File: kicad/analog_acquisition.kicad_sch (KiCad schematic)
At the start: 59 parts, among them J2 BNC_Isolated, J3 BNC_Isolated, J4 JST-XH 3-pin, J5 BNC_Isolated, J6 JST-XH 2-pin, J7 JST-XH 3-pin, T1 Transformer_SP_2S, T2 Transformer_SP_2S, T3 Transformer_SP_2S, U10 MCP6002, U11 MCP6002, U12 SN6501, U13 AMC1301, U4 MCP6002, U5 SN6501, U6 AMC1301, U7 MCP6002, U8 SN6501, U9 AMC1301

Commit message: fix: Resolve 4 Devin Review issues on analog_acquisition
1. Duplicate #PWR refs: renumbered 6 colliding GND symbols
   (#PWR36/37/38/40 duplicated across non-iso channels)
   to unique refs #PWR51-56

2. Transformer footprint+MPN: T1-T3 assigned
   Wuerth 750315371 (SN6501-compatible center-tapped
   transformer), footprint from KiCad stock library

3. Zero-length wires: removed 3 degenerate wires at
   hier_label positions for CO2/Temp/Hum channels

4. Missing MPN/Distributor_PN: added to D19-D24
   (BAT54,115 Schottky) and C28-C30 (GRM21BR61C106KE15L
   10uF MLCC)

ERC: Analog Acquisition = 0 violations, trace_net = 0 shorts
Co-Authored-By: Devin AI <158243242+devin-ai-integration[bot]@users.noreply.github.com>
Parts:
- C28, C29, C30: Distributor_PN (none) -> 490-6473-1-ND; MPN (none) -> GRM21BR61C106KE15L
- D19, D20, D21, D22, D23, D24: Distributor_PN (none) -> 1727-3752-1-ND; MPN (none) -> BAT54,115
- T1, T2, T3: footprint (none) -> Transformer_SMD:Transformer_Wuerth_750315371; Distributor_PN (none) -> 732-13596-1-ND; MPN (none) -> 750315371
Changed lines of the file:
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@@
     (property "Value" "Transformer_SP_2S" (at 243.84 71.12 0)
       (effects (font (size 1.27 1.27))))
-    (property "Footprint" "" (at 243.84 63.5 0)
+    (property "Footprint" "Transformer_SMD:Transformer_Wuerth_750315371" (at 243.84 63.5 0)
+      (effects (font (size 1.27 1.27)) hide))
+    (property "MPN" "750315371" (at 0 0 0)
+      (effects (font (size 1.27 1.27)) hide))
+    (property "Distributor_PN" "732-13596-1-ND" (at 0 0 0)
       (effects (font (size 1.27 1.27)) hide))
     (pin "1")
@@
     (property "Footprint" "Diode_SMD:D_SOD-123" (at 274.32 53.34 0)
       (effects (font (size 1.27 1.27)) hide))
+    (property "MPN" "BAT54,115" (at 0 0 0)
+      (effects (font (size 1.27 1.27)) hide))
+    (property "Distributor_PN" "1727-3752-1-ND" (at 0 0 0)
+      (effects (font (size 1.27 1.27)) hide))
     (pin "1")
     (pin "2")
@@
     (property "Footprint" "Diode_SMD:D_SOD-123" (at 274.32 73.66 0)
       (effects (font (size 1.27 1.27)) hide))
+    (property "MPN" "BAT54,115" (at 0 0 0)
+      (effects (font (size 1.27 1.27)) hide))
+    (property "Distributor_PN" "1727-3752-1-ND" (at 0 0 0)
+      (effects (font (size 1.27 1.27)) hide))
     (pin "1")
     (pin "2")
@@
       (effects (font (size 1.27 1.27))))
     (property "Footprint" "Capacitor_SMD:C_0805_2012Metric" (at 289.56 63.5 0)
+      (effects (font (size 1.27 1.27)) hide))
+    (property "MPN" "GRM21BR61C106KE15L" (at 0 0 0)
+      (effects (font (size 1.27 1.27)) hide))
+    (property "Distributor_PN" "490-6473-1-ND" (at 0 0 0)
       (effects (font (size 1.27 1.27)) hide))
     (pin "1")
@@
     (property "Value" "Transformer_SP_2S" (at 243.84 109.22 0)
       (effects (font (size 1.27 1.27))))
-    (property "Footprint" "" (at 243.84 101.6 0)
+    (property "Footprint" "Transformer_SMD:Transformer_Wuerth_750315371" (at 243.84 101.6 0)
+      (effects (font (size 1.27 1.27)) hide))
+    (property "MPN" "750315371" (at 0 0 0)
+      (effects (font (size 1.27 1.27)) hide))
+    (property "Distributor_PN" "732-13596-1-ND" (at 0 0 0)
       (effects (font (size 1.27 1.27)) hide))
     (pin "1")
@@
     (property "Footprint" "Diode_SMD:D_SOD-123" (at 274.32 91.44 0)
       (effects (font (size 1.27 1.27)) hide))
+    (property "MPN" "BAT54,115" (at 0 0 0)
+      (effects (font (size 1.27 1.27)) hide))
+    (property "Distributor_PN" "1727-3752-1-ND" (at 0 0 0)
+      (effects (font (size 1.27 1.27)) hide))
     (pin "1")
     (pin "2")
@@
     (property "Footprint" "Diode_SMD:D_SOD-123" (at 274.32 111.75999999999999 0)
       (effects (font (size 1.27 1.27)) hide))
+    (property "MPN" "BAT54,115" (at 0 0 0)
+      (effects (font (size 1.27 1.27)) hide))
+    (property "Distributor_PN" "1727-3752-1-ND" (at 0 0 0)
+      (effects (font (size 1.27 1.27)) hide))
     (pin "1")
     (pin "2")
@@
       (effects (font (size 1.27 1.27))))
     (property "Footprint" "Capacitor_SMD:C_0805_2012Metric" (at 289.56 101.6 0)
+      (effects (font (size 1.27 1.27)) hide))
+    (property "MPN" "GRM21BR61C106KE15L" (at 0 0 0)
+      (effects (font (size 1.27 1.27)) hide))
+    (property "Distributor_PN" "490-6473-1-ND" (at 0 0 0)
       (effects (font (size 1.27 1.27)) hide))
     (pin "1")
@@
     (property "Value" "Transformer_SP_2S" (at 243.84 185.42000000000002 0)
       (effects (font (size 1.27 1.27))))
-    (property "Footprint" "" (at 243.84 177.8 0)
+    (property "Footprint" "Transformer_SMD:Transformer_Wuerth_750315371" (at 243.84 177.8 0)
+      (effects (font (size 1.27 1.27)) hide))
+    (property "MPN" "750315371" (at 0 0 0)
+      (effects (font (size 1.27 1.27)) hide))
+    (property "Distributor_PN" "732-13596-1-ND" (at 0 0 0)
       (effects (font (size 1.27 1.27)) hide))
     (pin "1")
@@
     (property "Footprint" "Diode_SMD:D_SOD-123" (at 274.32 167.64000000000001 0)
       (effects (font (size 1.27 1.27)) hide))
+    (property "MPN" "BAT54,115" (at 0 0 0)
+      (effects (font (size 1.27 1.27)) hide))
+    (property "Distributor_PN" "1727-3752-1-ND" (at 0 0 0)
+      (effects (font (size 1.27 1.27)) hide))
     (pin "1")
     (pin "2")
@@
     (property "Footprint" "Diode_SMD:D_SOD-123" (at 274.32 187.96 0)
       (effects (font (size 1.27 1.27)) hide))
+    (property "MPN" "BAT54,115" (at 0 0 0)
+      (effects (font (size 1.27 1.27)) hide))
+    (property "Distributor_PN" "1727-3752-1-ND" (at 0 0 0)
+      (effects (font (size 1.27 1.27)) hide))
     (pin "1")
     (pin "2")
@@
     (property "Footprint" "Capacitor_SMD:C_0805_2012Metric" (at 289.56 177.8 0)
       (effects (font (size 1.27 1.27)) hide))
+    (property "MPN" "GRM21BR61C106KE15L" (at 0 0 0)
+      (effects (font (size 1.27 1.27)) hide))
+    (property "Distributor_PN" "490-6473-1-ND" (at 0 0 0)
+      (effects (font (size 1.27 1.27)) hide))
     (pin "1")
     (pin "2")
@@
   )
   (wire (pts (xy 99.06 127.0) (xy 162.56 127.0))
-    (stroke (width 0) (type default))
-  )
-  (wire (pts (xy 162.56 127.0) (xy 162.56 127.0))
     (stroke (width 0) (type default))
   )
@@
     (unit 1)
     (exclude_from_sim no) (in_bom no) (on_board no)
-    (property "Reference" "#PWR36" (at 46.99 208.27999999999997 0)
+    (property "Reference" "#PWR51" (at 46.99 208.27999999999997 0)
       (effects (font (size 1.27 1.27)) hide))
     (property "Value" "GND" (at 46.99 207.01 0)
@@
     (pin "1")
     (instances (project "nebula_qshield"
-      (path "/c6da75fc-541f-4933-b134-f5eb8982a11b/9688e820-0346-4732-9e7d-cc0365bc1e8b" (reference "#PWR36") (unit 1))))
+      (path "/c6da75fc-541f-4933-b134-f5eb8982a11b/9688e820-0346-4732-9e7d-cc0365bc1e8b" (reference "#PWR51") (unit 1))))
   )
   (wire (pts (xy 54.61 203.2) (xy 52.07 203.2))
@@
     (unit 1)
     (exclude_from_sim no) (in_bom no) (on_board no)
-    (property "Reference" "#PWR37" (at 68.58 217.17 0)
+    (property "Reference" "#PWR52" (at 68.58 217.17 0)
       (effects (font (size 1.27 1.27)) hide))
     (property "Value" "GND" (at 68.58 215.9 0)
@@
     (pin "1")
     (instances (project "nebula_qshield"
-      (path "/c6da75fc-541f-4933-b134-f5eb8982a11b/9688e820-0346-4732-9e7d-cc0365bc1e8b" (reference "#PWR37") (unit 1))))
+      (path "/c6da75fc-541f-4933-b134-f5eb8982a11b/9688e820-0346-4732-9e7d-cc0365bc1e8b" (reference "#PWR52") (unit 1))))
   )
   (wire (pts (xy 76.2 207.01) (xy 76.2 204.47))
@@
     (unit 1)
     (exclude_from_sim no) (in_bom no) (on_board no)
-    (property "Reference" "#PWR38" (at 76.2 219.70999999999998 0)
+    (property "Reference" "#PWR53" (at 76.2 219.70999999999998 0)
       (effects (font (size 1.27 1.27)) hide))
     (property "Value" "GND" (at 76.2 218.44 0)
@@
     (pin "1")
     (instances (project "nebula_qshield"
-      (path "/c6da75fc-541f-4933-b134-f5eb8982a11b/9688e820-0346-4732-9e7d-cc0365bc1e8b" (reference "#PWR38") (unit 1))))
+      (path "/c6da75fc-541f-4933-b134-f5eb8982a11b/9688e820-0346-4732-9e7d-cc0365bc1e8b" (reference "#PWR53") (unit 1))))
   )
   (wire (pts (xy 64.77 203.2) (xy 162.56 203.2))
     (stroke (width 0) (type default))
   )
-  (wire (pts (xy 162.56 203.2) (xy 162.56 203.2))
-    (stroke (width 0) (type default))
-  )
   (wire (pts (xy 20.32 238.76) (xy 22.86 238.76))
     (stroke (width 0) (type default))
@@
     (unit 1)
     (exclude_from_sim no) (in_bom no) (on_board no)
-    (property "Reference" "#PWR37" (at 17.78 243.84 0)
+    (property "Reference" "#PWR54" (at 17.78 243.84 0)
       (effects (font (size 1.27 1.27)) hide))
     (property "Value" "GND" (at 17.78 242.57000000000002 0)
@@
     (pin "1")
     (instances (project "nebula_qshield"
-      (path "/c6da75fc-541f-4933-b134-f5eb8982a11b/9688e820-0346-4732-9e7d-cc0365bc1e8b" (reference "#PWR37") (unit 1))))
+      (path "/c6da75fc-541f-4933-b134-f5eb8982a11b/9688e820-0346-4732-9e7d-cc0365bc1e8b" (reference "#PWR54") (unit 1))))
   )
   (wire (pts (xy 20.32 243.84) (xy 17.78 243.84))
@@
     (unit 1)
     (exclude_from_sim no) (in_bom no) (on_board no)
-    (property "Reference" "#PWR38" (at 46.99 246.38 0)
+    (property "Reference" "#PWR55" (at 46.99 246.38 0)
       (effects (font (size 1.27 1.27)) hide))
     (property "Value" "GND" (at 46.99 245.11 0)
@@
     (pin "1")
     (instances (project "nebula_qshield"
-      (path "/c6da75fc-541f-4933-b134-f5eb8982a11b/9688e820-0346-4732-9e7d-cc0365bc1e8b" (reference "#PWR38") (unit 1))))
+      (path "/c6da75fc-541f-4933-b134-f5eb8982a11b/9688e820-0346-4732-9e7d-cc0365bc1e8b" (reference "#PWR55") (unit 1))))
   )
   (wire (pts (xy 54.61 241.3) (xy 52.07 241.3))
@@
     (unit 1)
     (exclude_from_sim no) (in_bom no) (on_board no)
-    (property "Reference" "#PWR40" (at 68.58 255.26999999999998 0)
+    (property "Reference" "#PWR56" (at 68.58 255.26999999999998 0)
       (effects (font (size 1.27 1.27)) hide))
     (property "Value" "GND" (at 68.58 254.0 0)
@@
     (pin "1")
     (instances (project "nebula_qshield"
-      (path "/c6da75fc-541f-4933-b134-f5eb8982a11b/9688e820-0346-4732-9e7d-cc0365bc1e8b" (reference "#PWR40") (unit 1))))
+      (path "/c6da75fc-541f-4933-b134-f5eb8982a11b/9688e820-0346-4732-9e7d-cc0365bc1e8b" (reference "#PWR56") (unit 1))))
   )
   (wire (pts (xy 76.2 245.11) (xy 76.2 242.57000000000002))
@@
     (stroke (width 0) (type default))
   )
-  (wire (pts (xy 162.56 241.3) (xy 162.56 241.3))
-    (stroke (width 0) (type default))
-  )

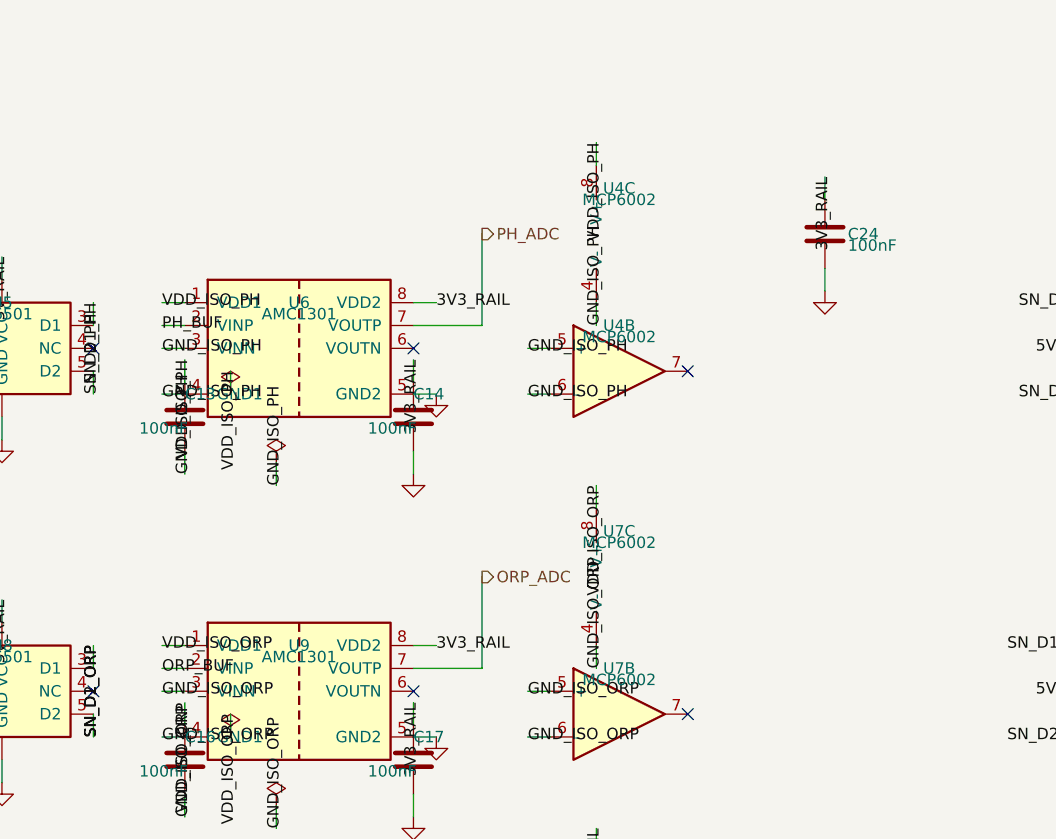
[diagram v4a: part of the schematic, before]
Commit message: fix: Add post-buffer resistive divider for pH/ORP input range (±250mV AMC1301)
Co-Authored-By: Devin AI <158243242+devin-ai-integration[bot]@users.noreply.github.com>
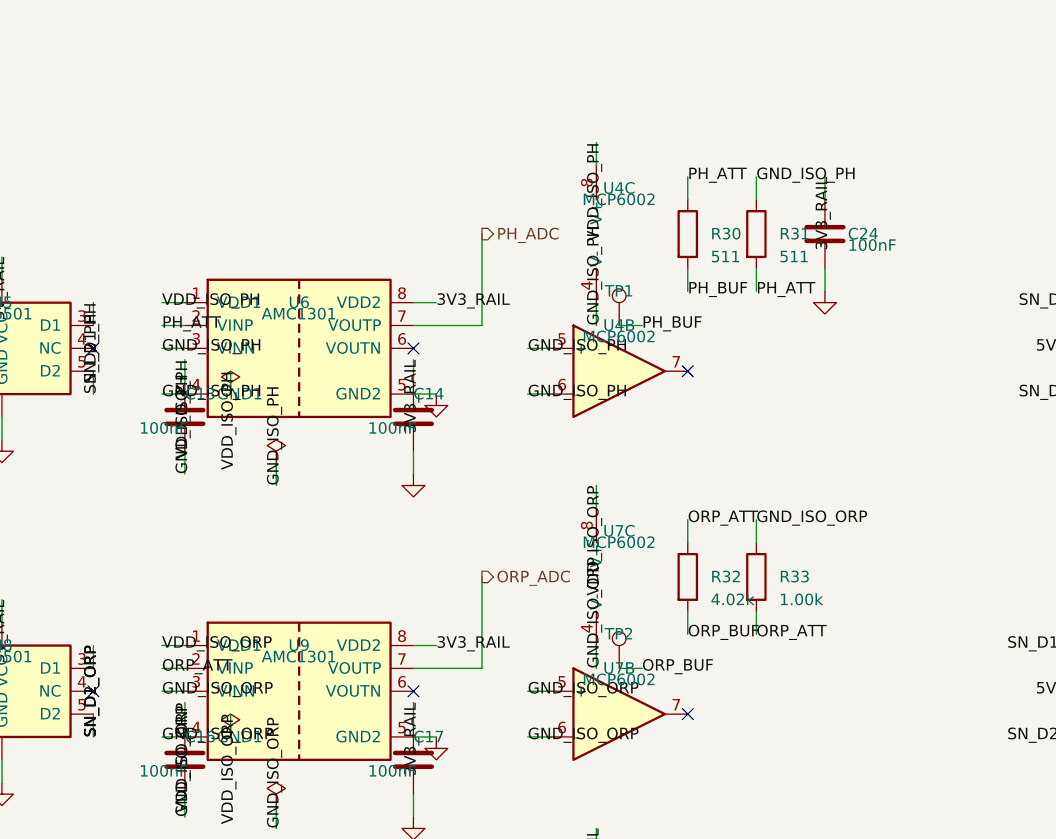
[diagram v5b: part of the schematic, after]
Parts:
- added R30, R31: 511, Resistor_SMD:R_0402_1005Metric, symbol Device:R
- added R32: 4.02k, Resistor_SMD:R_0402_1005Metric, symbol Device:R
- added R33: 1.00k, Resistor_SMD:R_0402_1005Metric, symbol Device:R
- added TP1, TP2: TestPoint, TestPoint:TestPoint_Pad_D1.5mm, symbol nebula_symbols:TestPoint
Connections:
- net GND_ISO_ORP: now also R33.1
- net GND_ISO_PH: now also R31.1
- net ORP_BUF: now also R32.2, TP2.1; no longer U9.2 (VINP)
- net PH_BUF: now also R30.2, TP1.1; no longer U6.2 (VINP)
- new net ORP_ATT: R32.1, R33.2, U9.2 (VINP)
- new net PH_ATT: R30.1, R31.2, U6.2 (VINP)
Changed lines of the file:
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@@
     (stroke (width 0) (type default))
   )
-  (label "PH_BUF" (at 126.99999999999999 60.96 0)
+  (label "PH_ATT" (at 126.99999999999999 60.96 0)
     (effects (font (size 1.27 1.27)))
   )
@@
     (stroke (width 0) (type default))
   )
-  (label "ORP_BUF" (at 126.99999999999999 99.06 0)
+  (label "ORP_ATT" (at 126.99999999999999 99.06 0)
     (effects (font (size 1.27 1.27)))
   )
@@
     (stroke (width 0) (type default))
   )
+  (symbol
+    (lib_id "Device:R")
+    (at 185.42 50.8 0)
+    (unit 1)
+    (exclude_from_sim no) (in_bom yes) (on_board yes)
+    (property "Reference" "R30" (at 187.95999999999998 50.8 0) (effects (font (size 1.27 1.27)) (justify left)))
+    (property "Value" "511" (at 187.95999999999998 53.339999999999996 0) (effects (font (size 1.27 1.27)) (justify left)))
+    (property "Footprint" "Resistor_SMD:R_0402_1005Metric" (at 185.42 50.8 90) (effects (font (size 1.27 1.27)) hide))
+    (property "Description" "pH input divider top (0.1%)" (at 185.42 50.8 0) (effects (font (size 1.27 1.27)) hide))
+    (pin "1") (pin "2")
+    (instances (project "nebula_qshield"
+      (path "/c6da75fc-541f-4933-b134-f5eb8982a11b/9688e820-0346-4732-9e7d-cc0365bc1e8b" (reference "R30") (unit 1))))
+  )
+  (wire (pts (xy 185.42 54.61) (xy 185.42 57.15)) (stroke (width 0) (type default)))
+  (label "PH_BUF" (at 185.42 57.15 0) (effects (font (size 1.27 1.27))))
+  (wire (pts (xy 185.42 46.989999999999995) (xy 185.42 44.449999999999996)) (stroke (width 0) (type default)))
+  (label "PH_ATT" (at 185.42 44.449999999999996 0) (effects (font (size 1.27 1.27))))
+  (symbol
+    (lib_id "Device:R")
+    (at 193.04 50.8 0)
+    (unit 1)
+    (exclude_from_sim no) (in_bom yes) (on_board yes)
+    (property "Reference" "R31" (at 195.57999999999998 50.8 0) (effects (font (size 1.27 1.27)) (justify left)))
+    (property "Value" "511" (at 195.57999999999998 53.339999999999996 0) (effects (font (size 1.27 1.27)) (justify left)))
+    (property "Footprint" "Resistor_SMD:R_0402_1005Metric" (at 193.04 50.8 90) (effects (font (size 1.27 1.27)) hide))
+    (property "Description" "pH input divider bottom (0.1%)" (at 193.04 50.8 0) (effects (font (size 1.27 1.27)) hide))
+    (pin "1") (pin "2")
+    (instances (project "nebula_qshield"
+      (path "/c6da75fc-541f-4933-b134-f5eb8982a11b/9688e820-0346-4732-9e7d-cc0365bc1e8b" (reference "R31") (unit 1))))
+  )
+  (wire (pts (xy 193.04 54.61) (xy 193.04 57.15)) (stroke (width 0) (type default)))
+  (label "PH_ATT" (at 193.04 57.15 0) (effects (font (size 1.27 1.27))))
+  (wire (pts (xy 193.04 46.989999999999995) (xy 193.04 44.449999999999996)) (stroke (width 0) (type default)))
+  (label "GND_ISO_PH" (at 193.04 44.449999999999996 0) (effects (font (size 1.27 1.27))))
+  (symbol
+    (lib_id "Device:R")
+    (at 185.42 88.9 0)
+    (unit 1)
+    (exclude_from_sim no) (in_bom yes) (on_board yes)
+    (property "Reference" "R32" (at 187.95999999999998 88.9 0) (effects (font (size 1.27 1.27)) (justify left)))
+    (property "Value" "4.02k" (at 187.95999999999998 91.44000000000001 0) (effects (font (size 1.27 1.27)) (justify left)))
+    (property "Footprint" "Resistor_SMD:R_0402_1005Metric" (at 185.42 88.9 90) (effects (font (size 1.27 1.27)) hide))
+    (property "Description" "ORP input divider top (0.1%)" (at 185.42 88.9 0) (effects (font (size 1.27 1.27)) hide))
+    (pin "1") (pin "2")
+    (instances (project "nebula_qshield"
+      (path "/c6da75fc-541f-4933-b134-f5eb8982a11b/9688e820-0346-4732-9e7d-cc0365bc1e8b" (reference "R32") (unit 1))))
+  )
+  (wire (pts (xy 185.42 92.71000000000001) (xy 185.42 95.25)) (stroke (width 0) (type default)))
+  (label "ORP_BUF" (at 185.42 95.25 0) (effects (font (size 1.27 1.27))))
+  (wire (pts (xy 185.42 85.09) (xy 185.42 82.55000000000001)) (stroke (width 0) (type default)))
+  (label "ORP_ATT" (at 185.42 82.55000000000001 0) (effects (font (size 1.27 1.27))))
+  (symbol
+    (lib_id "Device:R")
+    (at 193.04 88.9 0)
+    (unit 1)
+    (exclude_from_sim no) (in_bom yes) (on_board yes)
+    (property "Reference" "R33" (at 195.57999999999998 88.9 0) (effects (font (size 1.27 1.27)) (justify left)))
+    (property "Value" "1.00k" (at 195.57999999999998 91.44000000000001 0) (effects (font (size 1.27 1.27)) (justify left)))
+    (property "Footprint" "Resistor_SMD:R_0402_1005Metric" (at 193.04 88.9 90) (effects (font (size 1.27 1.27)) hide))
+    (property "Description" "ORP input divider bottom (0.1%)" (at 193.04 88.9 0) (effects (font (size 1.27 1.27)) hide))
+    (pin "1") (pin "2")
+    (instances (project "nebula_qshield"
+      (path "/c6da75fc-541f-4933-b134-f5eb8982a11b/9688e820-0346-4732-9e7d-cc0365bc1e8b" (reference "R33") (unit 1))))
+  )
+  (wire (pts (xy 193.04 92.71000000000001) (xy 193.04 95.25)) (stroke (width 0) (type default)))
+  (label "ORP_ATT" (at 193.04 95.25 0) (effects (font (size 1.27 1.27))))
+  (wire (pts (xy 193.04 85.09) (xy 193.04 82.55000000000001)) (stroke (width 0) (type default)))
+  (label "GND_ISO_ORP" (at 193.04 82.55000000000001 0) (effects (font (size 1.27 1.27))))
+  (symbol
+    (lib_id "nebula_symbols:TestPoint")
+    (at 177.8 60.96 0)
+    (unit 1)
+    (exclude_from_sim no) (in_bom yes) (on_board yes)
+    (property "Reference" "TP1" (at 177.8 57.15 0) (effects (font (size 1.27 1.27))))
+    (property "Value" "TestPoint" (at 177.8 55.88 0) (effects (font (size 1.27 1.27)) hide))
+    (property "Footprint" "TestPoint:TestPoint_Pad_D1.5mm" (at 177.8 60.96 0) (effects (font (size 1.27 1.27)) hide))
+    (pin "1")
+    (instances (project "nebula_qshield"
+      (path "/c6da75fc-541f-4933-b134-f5eb8982a11b/9688e820-0346-4732-9e7d-cc0365bc1e8b" (reference "TP1") (unit 1))))
+  )
+  (wire (pts (xy 177.8 60.96) (xy 180.34 60.96)) (stroke (width 0) (type default)))
+  (label "PH_BUF" (at 180.34 60.96 0) (effects (font (size 1.27 1.27))))
+  (symbol
+    (lib_id "nebula_symbols:TestPoint")
+    (at 177.8 99.06 0)
+    (unit 1)
+    (exclude_from_sim no) (in_bom yes) (on_board yes)
+    (property "Reference" "TP2" (at 177.8 95.25 0) (effects (font (size 1.27 1.27))))
+    (property "Value" "TestPoint" (at 177.8 93.98 0) (effects (font (size 1.27 1.27)) hide))
+    (property "Footprint" "TestPoint:TestPoint_Pad_D1.5mm" (at 177.8 99.06 0) (effects (font (size 1.27 1.27)) hide))
+    (pin "1")
+    (instances (project "nebula_qshield"
+      (path "/c6da75fc-541f-4933-b134-f5eb8982a11b/9688e820-0346-4732-9e7d-cc0365bc1e8b" (reference "TP2") (unit 1))))
+  )
+  (wire (pts (xy 177.8 99.06) (xy 180.34 99.06)) (stroke (width 0) (type default)))
+  (label "ORP_BUF" (at 180.34 99.06 0) (effects (font (size 1.27 1.27))))
 )
